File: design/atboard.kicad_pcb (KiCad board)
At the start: 2 copper layers, 36.8 x 53.3 mm, 8 parts, among them J1 AVR_SPI, J2 RIGHT_CONNECTOR, J3 LEFT_CONNECTOR, J4 POWER, U1 ATmega328-PU, Y1 8 MHz

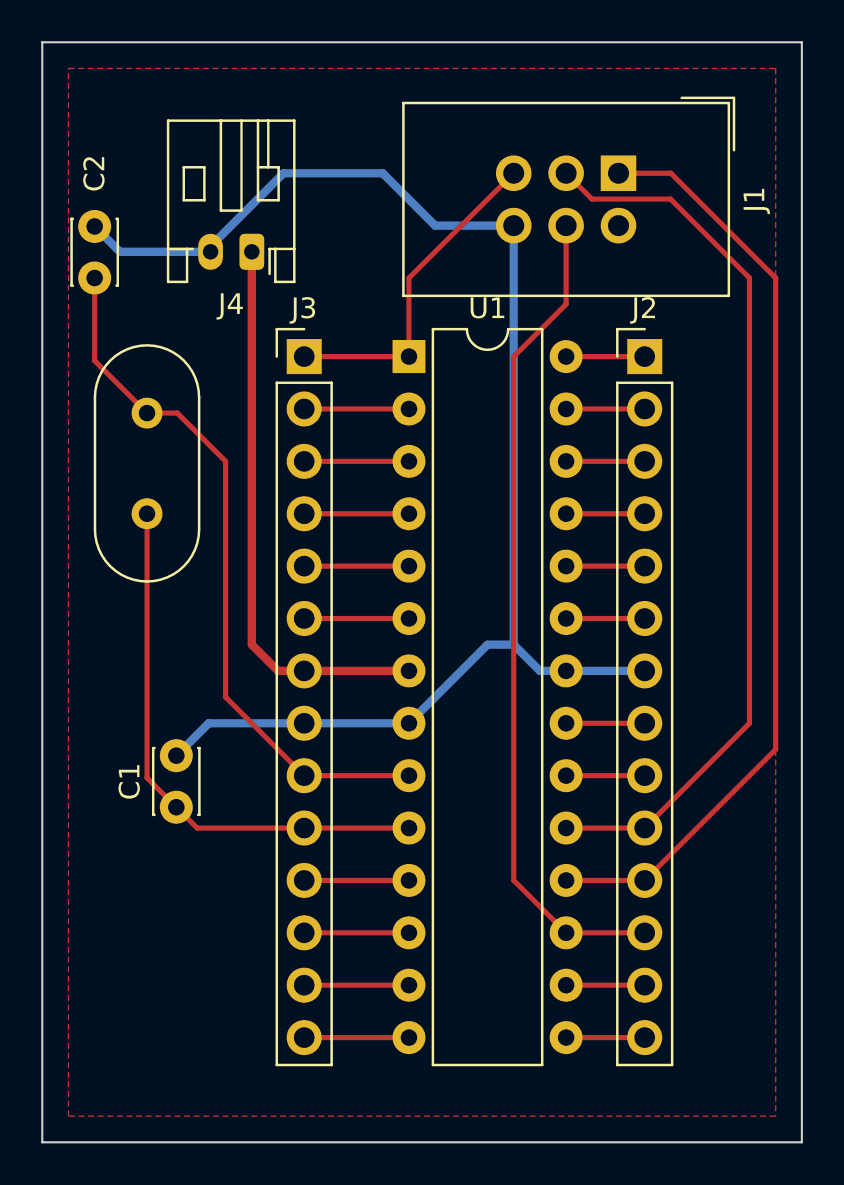
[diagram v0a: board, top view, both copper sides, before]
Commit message: added some text
still need to verufy breadboard width
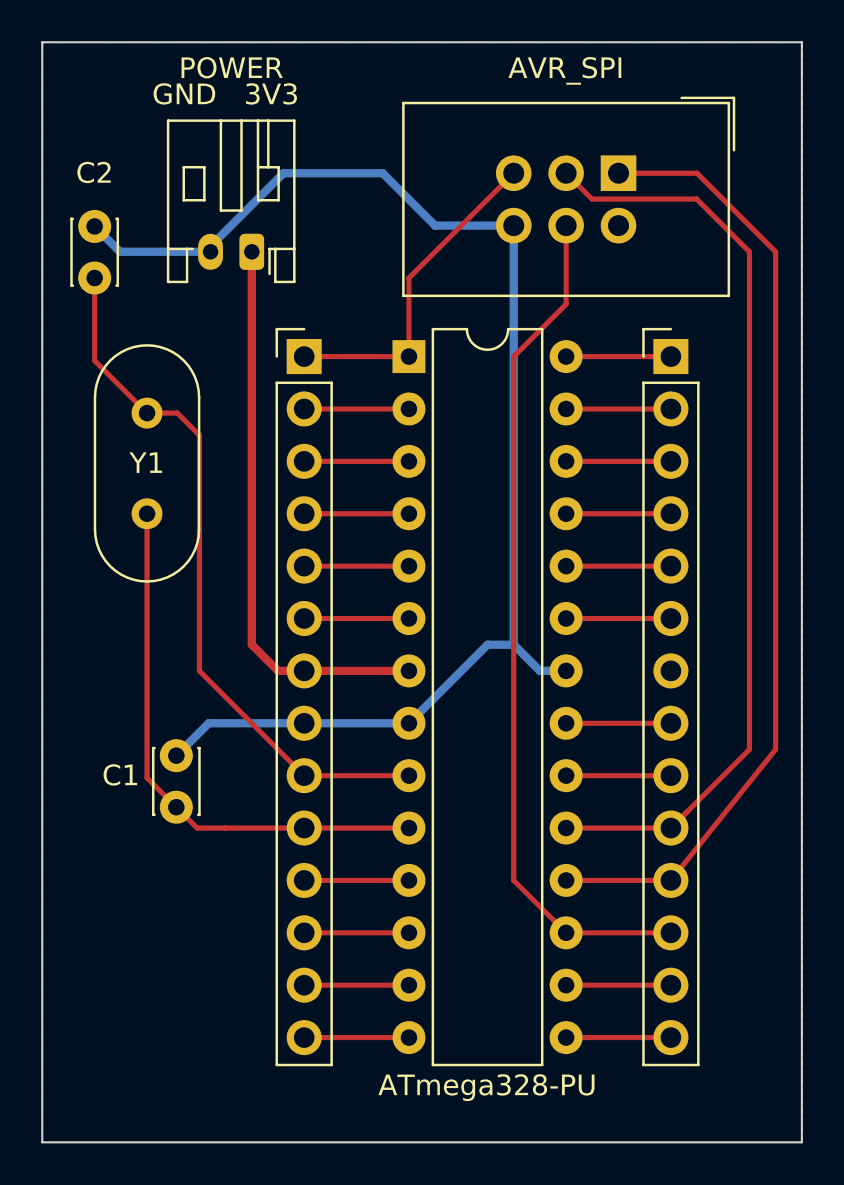
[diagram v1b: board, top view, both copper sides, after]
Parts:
- moved J2 1.27 mm to (94.0, 57.1)
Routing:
- net GND: track 69.7 -> 65.9 mm
- net /SCK: track 43.6 -> 46.3 mm
- net /MOSI: track 40.2 -> 41.5 mm
- net /28: track 3.81 -> 5.08 mm
- net /27: track 3.81 -> 5.08 mm
- net /26: track 3.81 -> 5.08 mm
- net /25: track 3.81 -> 5.08 mm
- net /24: track 3.81 -> 5.08 mm
- net /23: track 3.81 -> 5.08 mm
- net /21: track 3.81 -> 5.08 mm
- net /20: track 3.81 -> 5.08 mm
- net /16: track 3.81 -> 5.08 mm
- net /15: track 3.81 -> 5.08 mm
- net /MISO: track 45.4 -> 46.5 mm
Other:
- board text added: "BOTTOM"
- board text added: "GND 3V3"
